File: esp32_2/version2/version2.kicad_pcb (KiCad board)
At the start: 4 copper layers, 31 x 38.5 mm, 29 parts, among them J1 USB_C_Receptacle_USB2.0_16P, J2 Conn_01x08_Pin, J3 Conn_01x08_Pin, SW1 SW_Push, SW2 SW_Push, U1 USBLC6-2SC6, U2 AP2112K-3.3, U3 ESP32-C3-WROOM-02, Y1 Crystal

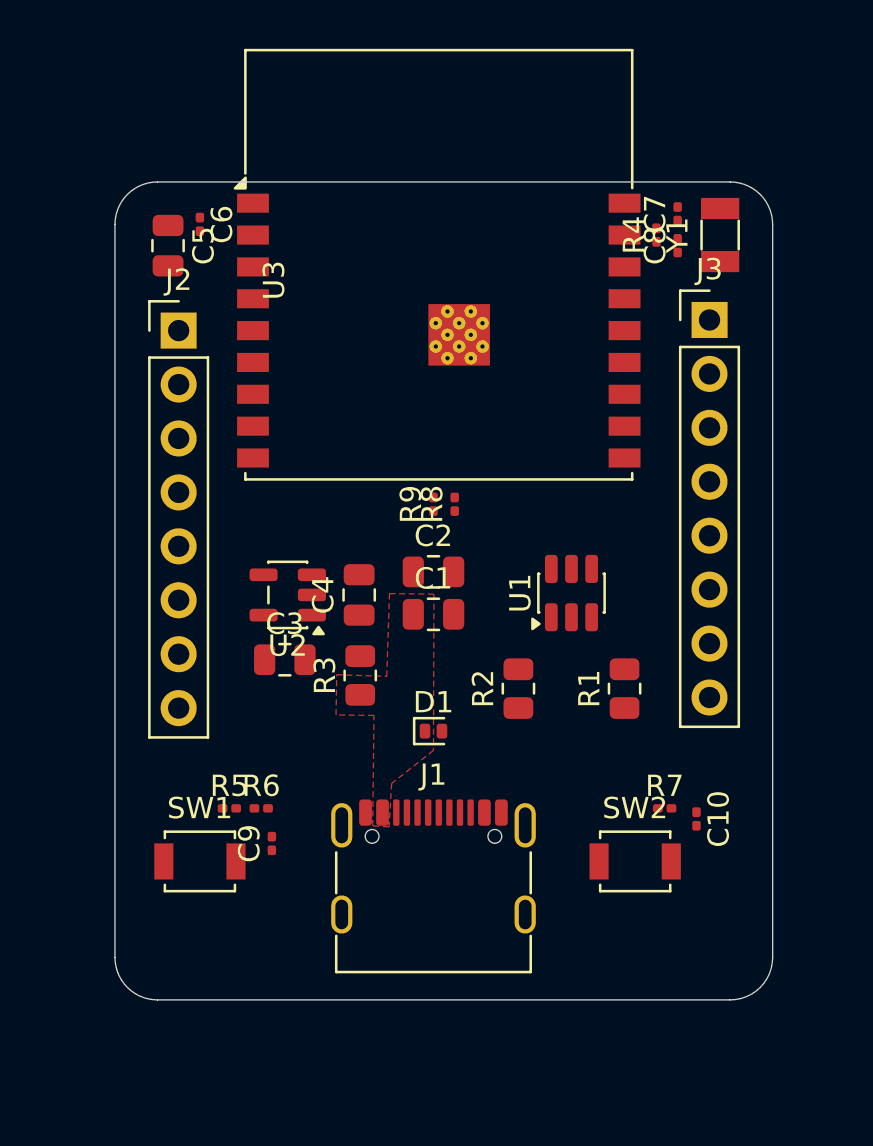
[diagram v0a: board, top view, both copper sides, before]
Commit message: added some more routing and copper filling for 5v and 3v3
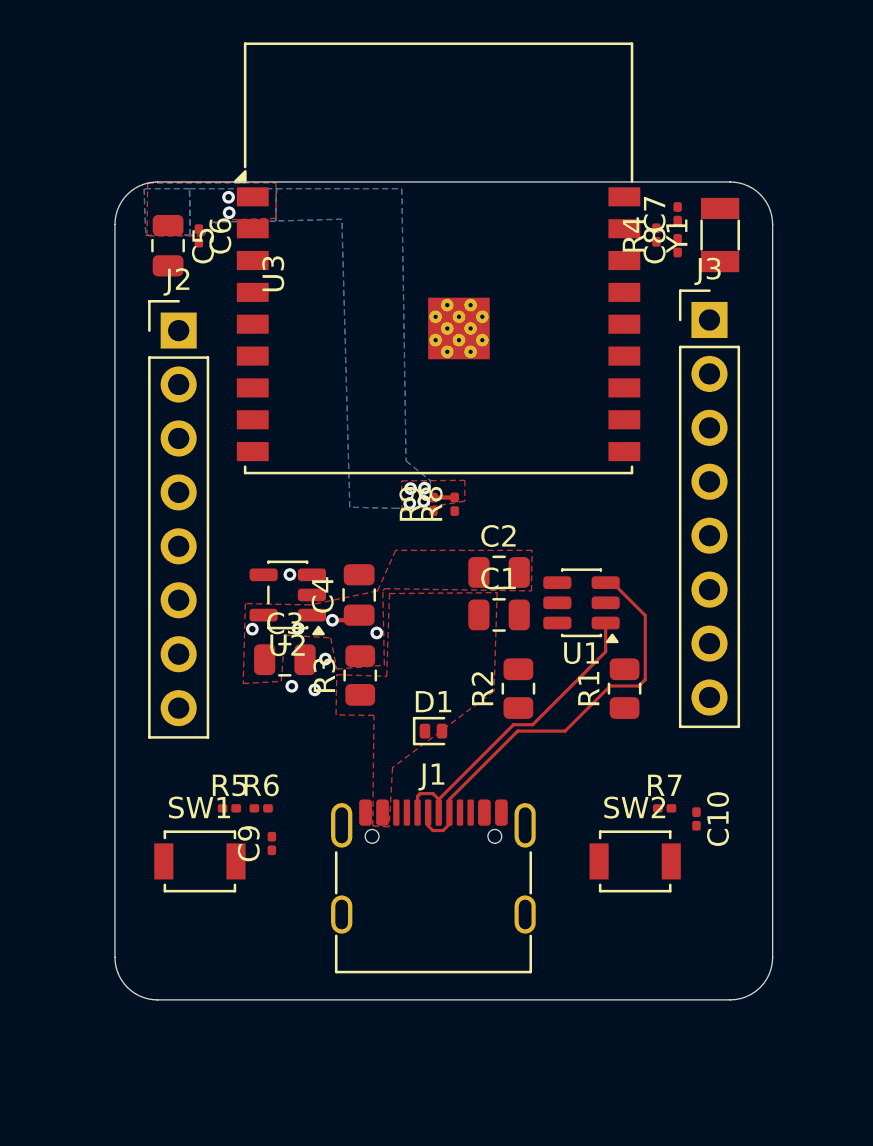
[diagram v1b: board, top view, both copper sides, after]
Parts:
- moved C1 3.09 mm to (90.6, 69.4)
- moved C2 3.09 mm to (90.6, 67.4)
- moved U1 0.66 mm to (94.5, 68.8), turned to 180 degrees
- moved C6 0.54 mm to (76.5, 51.5)
- moved U3 0.30 mm to (87.7, 55.7)
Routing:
- net /D+: track 0.00 -> 20.1 mm
- net /D-: track 0.00 -> 14.7 mm
- net +5V: track 0.00 -> 1.36 mm, vias 0 -> 5
- net +3V3: track 0.00 -> 1.00 mm, vias 0 -> 6
- net IO9: vias 0 -> 3
- added copper zone on B.Cu, net +3V3
- added copper zone on F.Cu, net +3V3
- added copper zone on F.Cu, net +5V

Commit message: fixed up some other basic routing issues i hate this
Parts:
- added G***: LOGO, LOGO, F.Cu at (87.4, 73.2)

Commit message: more routing more vias more visas (not)
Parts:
- C7, C8, R4, Y1: moved to B.Cu
- moved Y1 8.79 mm to (92.2, 52.3)
- moved C7 5.20 mm to (93.9, 51.5)
- moved C8 5.20 mm to (93.9, 53.0), turned to -90 degrees
- moved R4 3.32 mm to (94.8, 52.4), turned to -90 degrees
- moved R2 1.22 mm to (90.6, 72.0)
- moved J2 0.96 mm to (74.5, 55.9)
- moved D1 0.95 mm to (88.2, 74.2)
- moved C1 0.81 mm to (89.8, 69.3)
- moved C2 0.81 mm to (89.8, 67.3)
- moved J3 0.72 mm to (101.2, 55.6)
- moved U1 0.44 mm to (94.9, 69.0), turned to 0 degrees
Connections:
- U3 pad 11: IO13 -> RXD
- U3 pad 12: IO14 -> TXD
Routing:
- net IO10: track 0.00 -> 18.5 mm, vias 0 -> 1
- net IO7: track 0.00 -> 17.9 mm, vias 0 -> 1
- net IO6: track 0.00 -> 17.4 mm, vias 0 -> 1
- net USB_D+: track 0.00 -> 16.9 mm
- net USB_D-: track 0.00 -> 16.2 mm
- net RXD: track 0.00 -> 15.1 mm, vias 0 -> 1
- net IO5: track 0.00 -> 14.4 mm
- net TXD: track 0.00 -> 14.0 mm, vias 0 -> 1
- net IO4: track 0.00 -> 13.9 mm
- net EN: track 0.00 -> 12.6 mm
- net IO8: track 0.00 -> 11.1 mm
- net Net-(J1-CC2): track 0.00 -> 9.65 mm
- net Net-(U3-IO0): track 0.00 -> 8.42 mm, vias 0 -> 1
- net Net-(J1-CC1): track 0.00 -> 8.10 mm
- net /D+: track 20.1 -> 12.0 mm
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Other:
- board text added: "add in GND (IO9 = GND) near the vias because if something changes and the pcb needs to find ground, the current will spread throughout the entire pcb and can cause serious damage. better to have a GND pin right there in case something happens"

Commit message: finished routing
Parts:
- moved C9 6.29 mm to (73.7, 79.3), turned to -90 degrees
- moved R6 4.59 mm to (74.8, 79.0), turned to 180 degrees
- moved R5 1.62 mm to (76.3, 78.9)
- moved R7 0.21 mm to (98.5, 78.7), turned to 180 degrees
- moved C10 0.12 mm to (100.0, 79.0)
- turned SW1 to 180 degrees
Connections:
- C1 pad 2: IO9 -> GND
- C10 pad 2: IO9 -> GND
- C2 pad 2: IO9 -> GND
- C3 pad 2: IO9 -> GND
- C4 pad 2: IO9 -> GND
- C5 pad 2: IO9 -> GND
- C6 pad 2: IO9 -> GND
- C7 pad 2: IO9 -> GND
- C8 pad 2: IO9 -> GND
- C9 pad 2: IO9 -> GND
- D1 pad 2: IO9 -> GND
- J1 pad A1: IO9 -> GND
- J1 pad A12: IO9 -> GND
- J1 pad B1: IO9 -> GND
- J1 pad B12: IO9 -> GND
- J1 pad SH: IO9 -> GND
- J2 pad 2: IO9 -> GND
- J3 pad 2: IO9 -> GND
- J3 pad 4: IO9 -> GND
- J3 pad 7: IO9 -> GND
- R1 pad 2: IO9 -> GND
- R2 pad 2: IO9 -> GND
- R5 pad 1: IO9 -> Net-(R5-Pad1)
- R6 pad 1: IO9 -> Net-(R5-Pad1)
- SW1 pad 1: IO9 -> GND
- SW1 pad 2: IO9 -> Net-(R5-Pad1)
- SW2 pad 1: IO9 -> GND
- U1 pad 2: IO9 -> GND
- U2 pad 2: IO9 -> GND
- U3 pad 11: RXD -> IO13
- U3 pad 12: TXD -> IO14
- U3 pad 19: IO9 -> GND
- U3 pad 9: IO9 -> GND
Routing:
- net +3V3: track 1.00 -> 54.1 mm, vias 6 -> 8
- net IO9: track 0.00 -> 47.3 mm, vias 10 -> 1
- net EN: track 12.6 -> 32.5 mm, vias 0 -> 1
- net IO2: track 0.00 -> 15.9 mm
- net IO3: track 0.00 -> 9.39 mm
- net Net-(R5-Pad1): track 0.00 -> 3.06 mm
- net IO10: track 18.5 -> 16.6 mm
- net RXD: track 15.1 -> 13.5 mm
- net TXD: track 14.0 -> 12.9 mm
- net GND: vias 0 -> 10
- added copper zone on B.Cu, net +5V
- added copper zone on B.Cu, net GND
- added copper zone on F.Cu, net GND
- added copper zone on In1.Cu, net GND
- added copper zone on In2.Cu, net GND
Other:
- board text added: "add in GND near the vias because if something changes and the pcb needs to find ground, the current will spread throughout the entire pcb and can cause serious damage. better to have a GND pin right there in case something happens"
- board text removed: "add in GND (IO9 = GND) near the vias because if something changes and the pcb needs to find ground, the current will spread throughout the entire pcb and can cause serious damage. better to have a GND pin right there in case something happens"

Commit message: finished routing and finished pcb design!
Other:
- board text added: "5V GND IO3 GND TXD RXD GND IO10"
- board text added: "BOOT"
- board text added: "IO9 IO7 IO6 IO5 IO4 EN GND 3.3V"
- board text added: "Made by Shelley For Hack Club #Fallout"
- board text added: "RESET"
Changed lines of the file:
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@@
 			(at 0 -2.5 0)
 			(layer "F.SilkS")
+			(hide yes)
 			(effects
 				(font
@@
 			(at 0 2.5 0)
 			(layer "F.Fab")
+			(hide yes)
 			(effects
 				(font
@@
 			(at 0 -1.05 90)
 			(layer "F.SilkS")
+			(hide yes)
 			(effects
 				(font
@@
 			(at 0 2.5 0)
 			(layer "F.Fab")
+			(hide yes)
 			(effects
 				(font
@@
 		)
 	)
+	(gr_rect
+		(start 79.66 58.23)
+		(end 96.47 65.11)
+		(stroke
+			(width 0.1)
+			(type default)
+		)
+		(fill no)
+		(layer "B.SilkS")
+	)
 	(gr_arc
 		(start 72.5 51)
@@
 		(layer "Edge.Cuts")
 	)
+	(gr_text "IO9 IO7 IO6  IO5 IO4 EN GND 3.3V"
+		(at 77.12 74.68 90)
+		(layer "F.SilkS")
+		(effects
+			(font
+				(size 0.75 0.75)
+				(thickness 0.1)
+			)
+			(justify left bottom)
+		)
+	)
+	(gr_text "5V GND IO3 GND TXD RXD GND IO10"
+		(at 99.13 54.74 270)
+		(layer "F.SilkS")
+		(effects
+			(font
+				(size 0.75 0.75)
+				(thickness 0.1)
+			)
+			(justify left bottom)
+		)
+	)
+	(gr_text "RESET"
+		(at 75.249801 77.296137 0)
+		(layer "F.SilkS")
+		(effects
+			(font
+				(size 1 1)
+				(thickness 0.2)
+				(bold yes)
+			)
+			(justify left bottom)
+		)
+	)
+	(gr_text "BOOT"
+		(at 95.869635 77.940696 0)
+		(layer "F.SilkS")
+		(effects
+			(font
+				(size 1 1)
+				(thickness 0.2)
+				(bold yes)
+			)
+			(justify left bottom)
+		)
+	)
+	(gr_text "Made by Shelley\nFor Hack Club\n#Fallout"
+		(at 81.44 63.97 0)
+		(layer "B.SilkS")
+		(effects
+			(font
+				(size 1 1)
+				(thickness 0.1)
+			)
+			(justify right bottom mirror)
+		)
+	)
 	(gr_text "add in GND near the vias\nbecause if something changes and the pcb\nneeds to find ground, the current will\nspread throughout the entire pcb and \ncan cause serious damage. better to have\na GND pin right there in case something\nhappens"

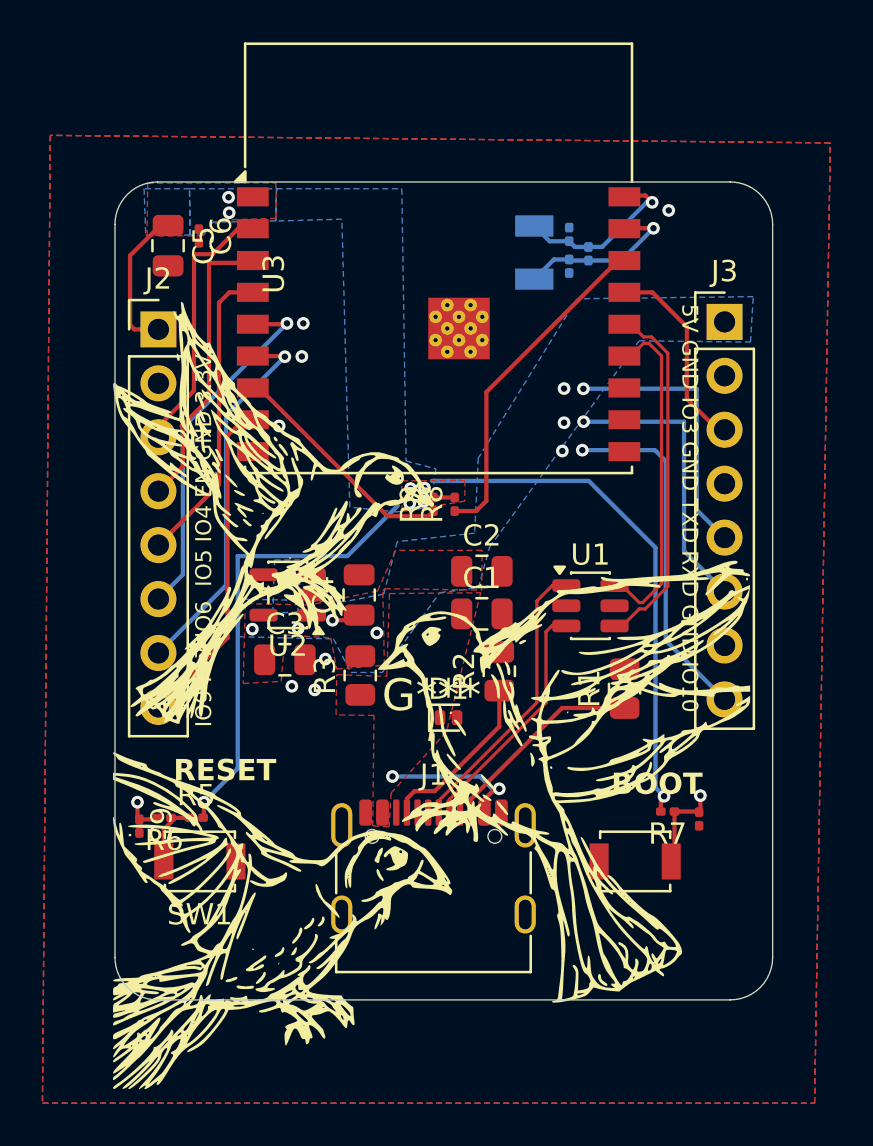
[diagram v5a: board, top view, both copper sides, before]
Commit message: edited mounting holes
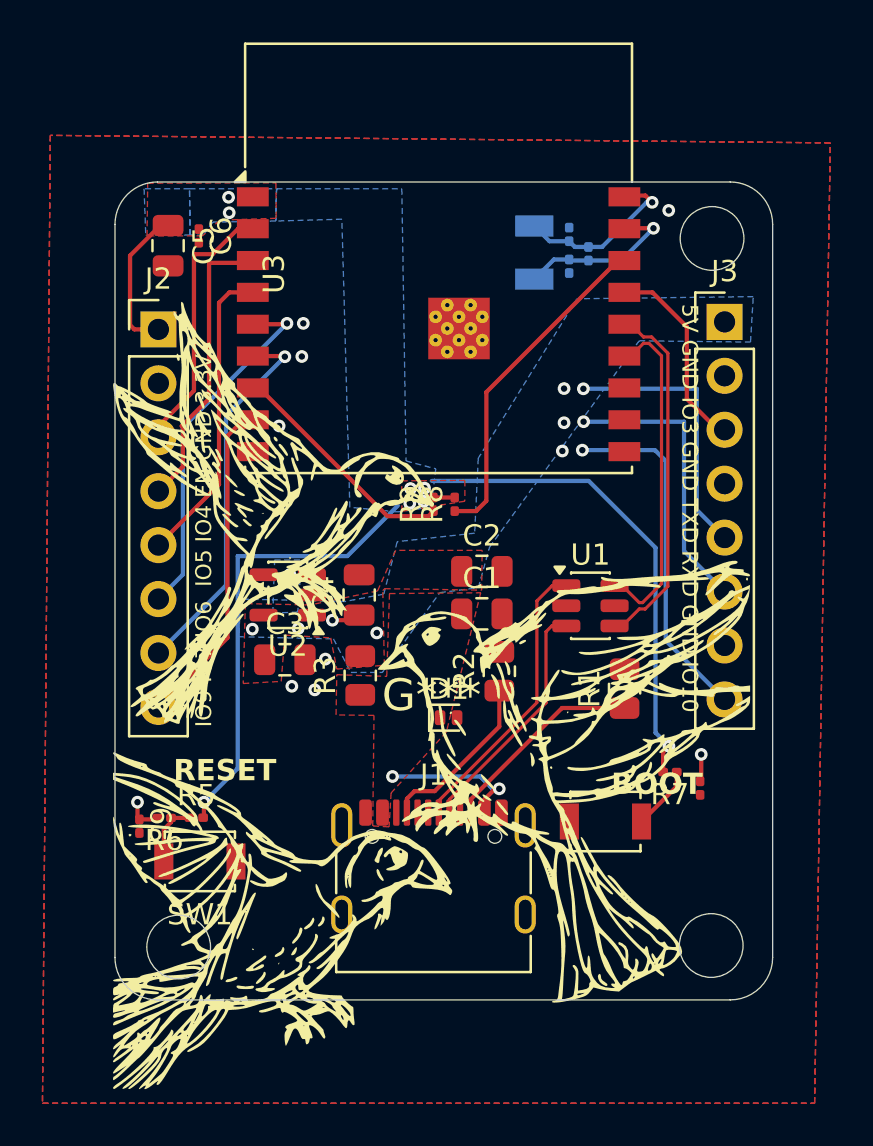
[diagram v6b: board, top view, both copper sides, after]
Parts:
- moved SW2 2.34 mm to (95.6, 79.1)
- moved R7 1.86 mm to (98.6, 76.8)
- moved C10 1.46 mm to (100.1, 77.5)
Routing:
- net +3V3: track 54.1 -> 52.4 mm
- net IO9: track 47.3 -> 46.7 mm
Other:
- outline, holes or cut-outs redrawn

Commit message: oops some formatting stuff
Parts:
- moved SW2 1.55 mm to (95.8, 80.7)
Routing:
- net IO9: track 46.7 -> 48.1 mm
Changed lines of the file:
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@@
 	(footprint "Button_Switch_SMD:SW_SPST_B3U-1000P"
 		(layer "F.Cu")
-		(at 95.6 79.12)
+		(at 95.81 80.66)
 		(descr "Ultra-small-sized Tactile Switch with High Contact Reliability, Top-actuated Model, without Ground Terminal, without Boss")
 		(tags "Tactile Switch")
@@
 			(at 0 -1.05 0)
 			(layer "F.SilkS")
+			(hide yes)
 			(effects
 				(font
@@
 			(at 0 -1.05 0)
 			(layer "F.SilkS")
+			(hide yes)
 			(effects
 				(font
@@
 	)
 	(gr_text "RESET"
-		(at 75.249801 77.296137 0)
+		(at 74.59 77.75 0)
 		(layer "F.SilkS")
 		(effects
@@
 	)
 	(gr_text "BOOT"
-		(at 95.869635 77.940696 0)
+		(at 93.83 77.72 0)
 		(layer "F.SilkS")
 		(effects
@@
 	)
 	(segment
-		(start 98.955 76.79)
-		(end 98.955 77.465)
+		(start 77.8 60.96)
+		(end 78.56 60.2)
 		(width 0.2)
 		(layer "F.Cu")
@@
 	)
 	(segment
-		(start 77.8 60.96)
-		(end 78.56 60.2)
+		(start 78.56 60.2)
+		(end 78.99 60.2)
 		(width 0.2)
 		(layer "F.Cu")
@@
 	)
 	(segment
-		(start 78.56 60.2)
-		(end 78.99 60.2)
+		(start 98.955 79.215)
+		(end 97.51 80.66)
 		(width 0.2)
 		(layer "F.Cu")
@@
 	)
 	(segment
-		(start 74.546145 73.722333)
-		(end 77.8 70.468478)
+		(start 98.955 76.79)
+		(end 98.955 79.215)
 		(width 0.2)
 		(layer "F.Cu")
@@
 	)
 	(segment
-		(start 100.11 75.96)
-		(end 100.11 77.175)
+		(start 74.546145 73.722333)
+		(end 77.8 70.468478)
 		(width 0.2)
 		(layer "F.Cu")
@@
 	)
 	(segment
-		(start 98.955 77.465)
-		(end 97.3 79.12)
+		(start 100.11 75.96)
+		(end 100.11 77.175)
 		(width 0.2)
 		(layer "F.Cu")
